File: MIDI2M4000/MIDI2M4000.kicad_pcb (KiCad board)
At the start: 2 copper layers, 74.9 x 56.5 mm, 42 parts, among them J1 MIDI_THRU, J2 BOOT_JMP, J3 MIDI_IN, J4 DEBUG, J5 USER PORT, J6 5V_POWER, J7 SPARE_PINS, SW1 RESET, SW2 SET_CHAN, U1 74LV14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

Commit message: Added another decoupler for optoisolator.
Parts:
- removed G***: LOGO, KiCad:CCBYSA
- removed REF**: OSHW-Logo2_7.3x6mm_SilkScreen, Symbol:OSHW-Logo2_7.3x6mm_SilkScreen
- added C13: 0.1uF, Capacitor_SMD:C_0805_2012Metric, F.Cu at (134.1, 66.3)
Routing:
- net +3V3: track 177.1 -> 179.3 mm
- net GND: vias 119 -> 117

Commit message: Logos back on PCB
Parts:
- added G***: LOGO, Symbol:CCBYSA, F.Cu at (134.6, 78.7)
- added REF**: OSHW-Logo2_7.3x6mm_SilkScreen, Symbol:OSHW-Logo2_7.3x6mm_SilkScreen, F.Cu at (166.4, 68.6)

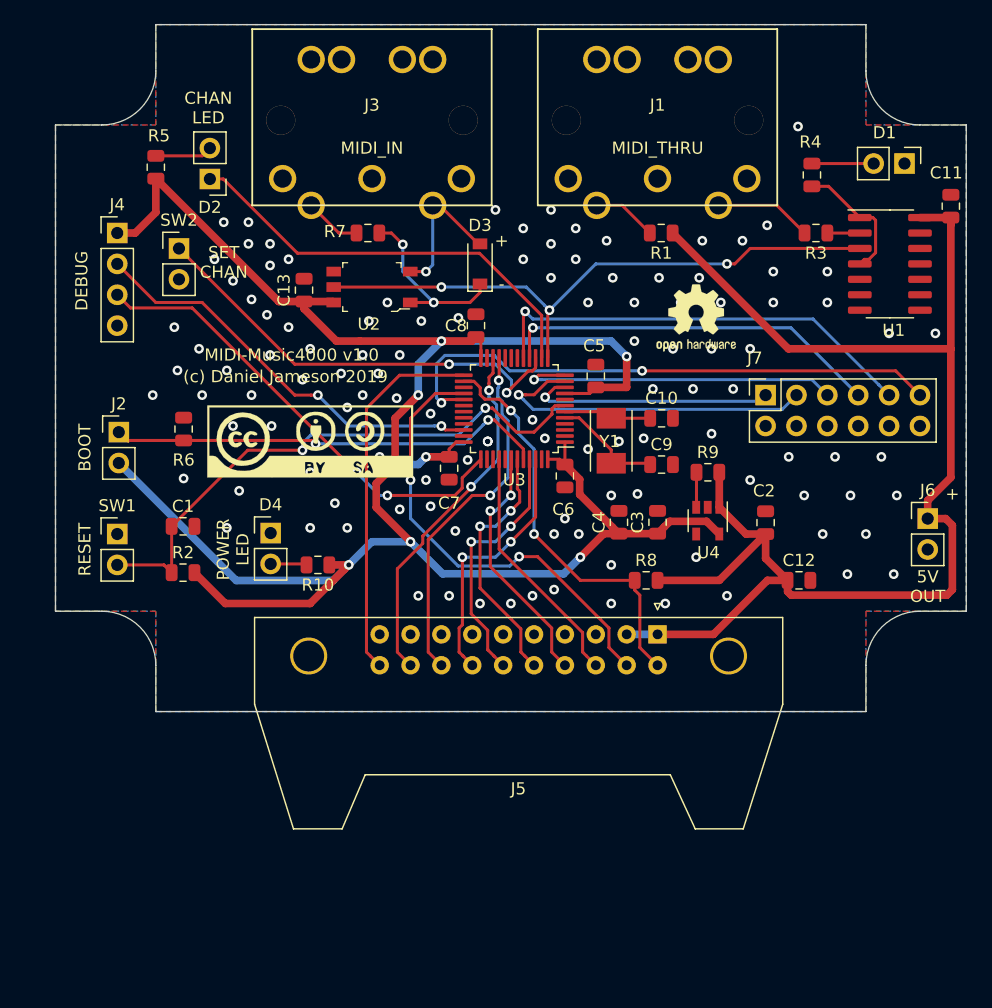
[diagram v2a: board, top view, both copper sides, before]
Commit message: Shrunk PCB, v1.1
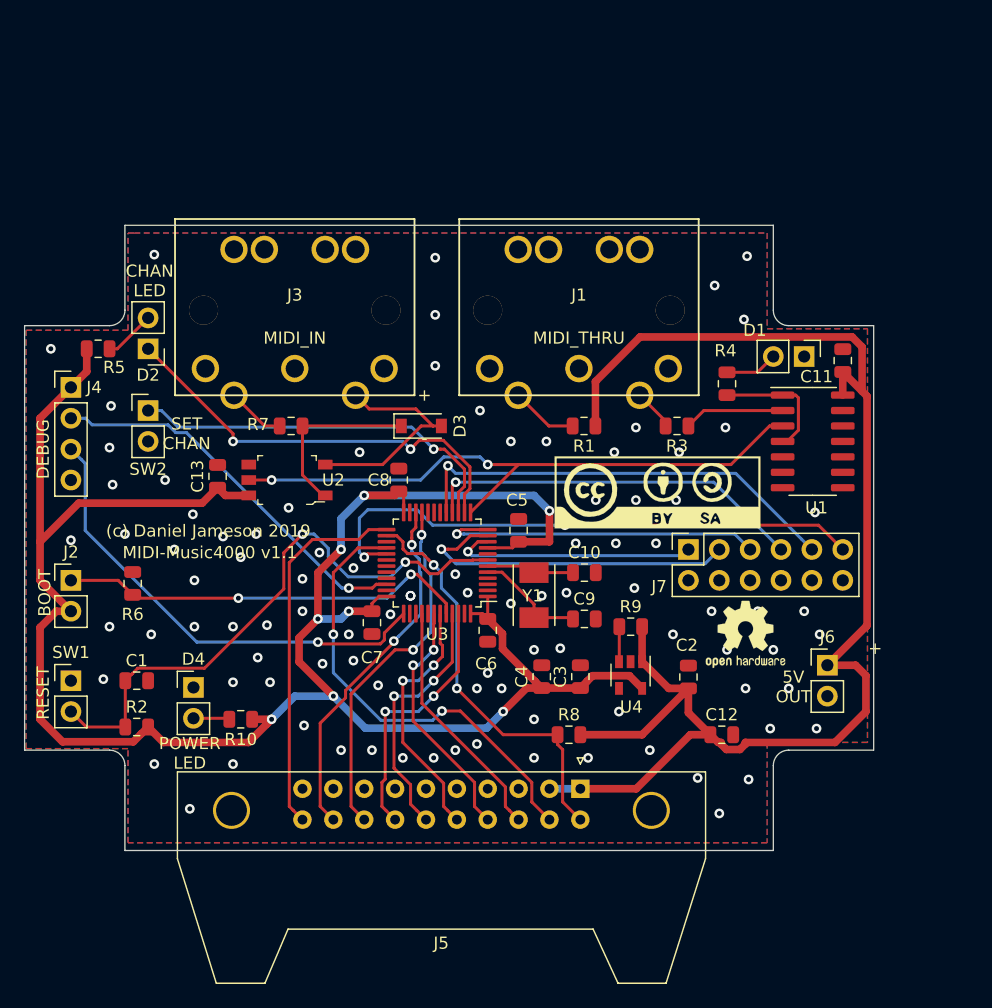
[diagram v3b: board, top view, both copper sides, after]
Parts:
- moved G*** 28.9 mm to (163.2, 82.9)
- moved REF** 26.4 mm to (170.4, 94.6)
- moved R3 19.6 mm to (164.8, 77.5)
- moved R4 18.5 mm to (168.9, 74.0)
- moved D1 17.9 mm to (175.3, 71.8)
- moved U2 17.3 mm to (132.7, 81.9)
- moved R1 17.1 mm to (157.1, 77.5)
- moved R7 17.1 mm to (133.0, 77.5)
- moved J1 16.9 mm to (156.7, 67.7)
- moved C13 16.9 mm to (127.0, 81.6)
- moved J3 16.9 mm to (133.3, 67.7)
- moved U1 15.9 mm to (176.0, 78.7)
- moved R5 15.7 mm to (117.2, 71.1), turned to 0 degrees
- moved C11 15.5 mm to (178.4, 72.1)
- moved D2 14.9 mm to (121.3, 71.1)
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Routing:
- net Net-(D3-Pad2): track 12.2 -> 18.3 mm, vias 1 -> 0
- net Net-(R3-Pad1): track 2.67 -> 8.28 mm
- net CH_BUTTON: track 37.1 -> 31.8 mm, vias 2 -> 1
- net Net-(J1-Pad5): track 8.04 -> 3.41 mm
- net +5V: track 115.0 -> 118.3 mm
- net BOOT: track 37.7 -> 34.4 mm
- net SWDIO: track 34.2 -> 31.9 mm, vias 2 -> 1
- net MIDI_DATA: track 50.2 -> 51.9 mm, vias 3 -> 2
- net Net-(C1-Pad1): track 47.2 -> 48.6 mm
- net +3V3: track 179.3 -> 178.1 mm
- net Net-(D1-Pad2): track 5.08 -> 4.35 mm
- net Net-(D3-Pad1): track 14.9 -> 14.7 mm, vias 2 -> 0
- net SWCLK: track 38.5 -> 38.6 mm, vias 2 -> 1
- net CH_LED: track 35.5 -> 35.4 mm, vias 0 -> 2
- net GND: vias 117 -> 96
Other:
- board size 74.9 x 56.5 mm -> 69.8 x 51.4 mm
- board text added: "MIDI-Music4000 v1.1"
- board text removed: "MIDI-Music4000 v1.0"
